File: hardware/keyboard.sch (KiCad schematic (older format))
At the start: 140 parts

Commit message: WIP schematic + PCB design
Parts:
- removed D? (x64): D, symbol D
- removed S? (x63): SPST, symbol SPST
- added D10, D11, D12, D13, D14, D15, D16, D17, D18, D19, D20, D21, D22, D23, D24, D25, D26, D27, D28, D29, D3, D30, D31, D32, D33, D34, D35, D36, D37, D38, D39, D4, D40, D41, D42, D43, D44, D45, D46, D47, D48, D49, D5, D50, D51, D52, D53, D54, D55, D56, D57, D58, D59, D6, D60, D61, D62, D63, D64, D65, D66, D7, D8, D9: D_Small, Diodes_SMD:D_1206, symbol D_Small
- added S10, S11, S12, S13, S14, S15, S16, S17, S18, S19, S2, S20, S21, S22, S23, S24, S25, S26, S27, S28, S29, S3, S30, S31, S32, S33, S34, S35, S36, S37, S38, S39, S4, S40, S41, S42, S43, S44, S45, S46, S47, S48, S49, S5, S50, S51, S52, S53, S54, S55, S56, S57, S58, S59, S6, S60, S61, S62, S63, S64, S7, S8, S9: SPST, keyboard-modules:CHERRY_PCB_100H, symbol SPST
- C1, C2, C3: renamed from C?; footprint (none) -> Capacitors_SMD:C_1206_HandSoldering
- D1: renamed from D?; footprint (none) -> LEDs:LED_1206
- D2: renamed from D?; footprint (none) -> Diodes_SMD:D_1206
- F1: renamed from F?; footprint (none) -> Fuse_Holders_and_Fuses:Fuse_SMD1206_HandSoldering
- J1: renamed from J?; footprint (none) -> Connectors_USB:USB_Micro-B_Molex-105017-0001
- R1, R2, R3: renamed from R?; footprint (none) -> Resistors_SMD:R_1206_HandSoldering
- S1: renamed from S?; footprint (none) -> keyboard-modules:CHERRY_PCB_100H
- U1: renamed from U?; footprint TQFP44 -> Housings_QFP:TQFP-44_10x10mm_Pitch0.8mm
- Y1: renamed from Y?; footprint (none) -> Crystals:Crystal_SMD_2012-2pin_2.0x1.2mm_HandSoldering
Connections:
- wire segments 168 -> 360
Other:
- moved on the sheet: S1

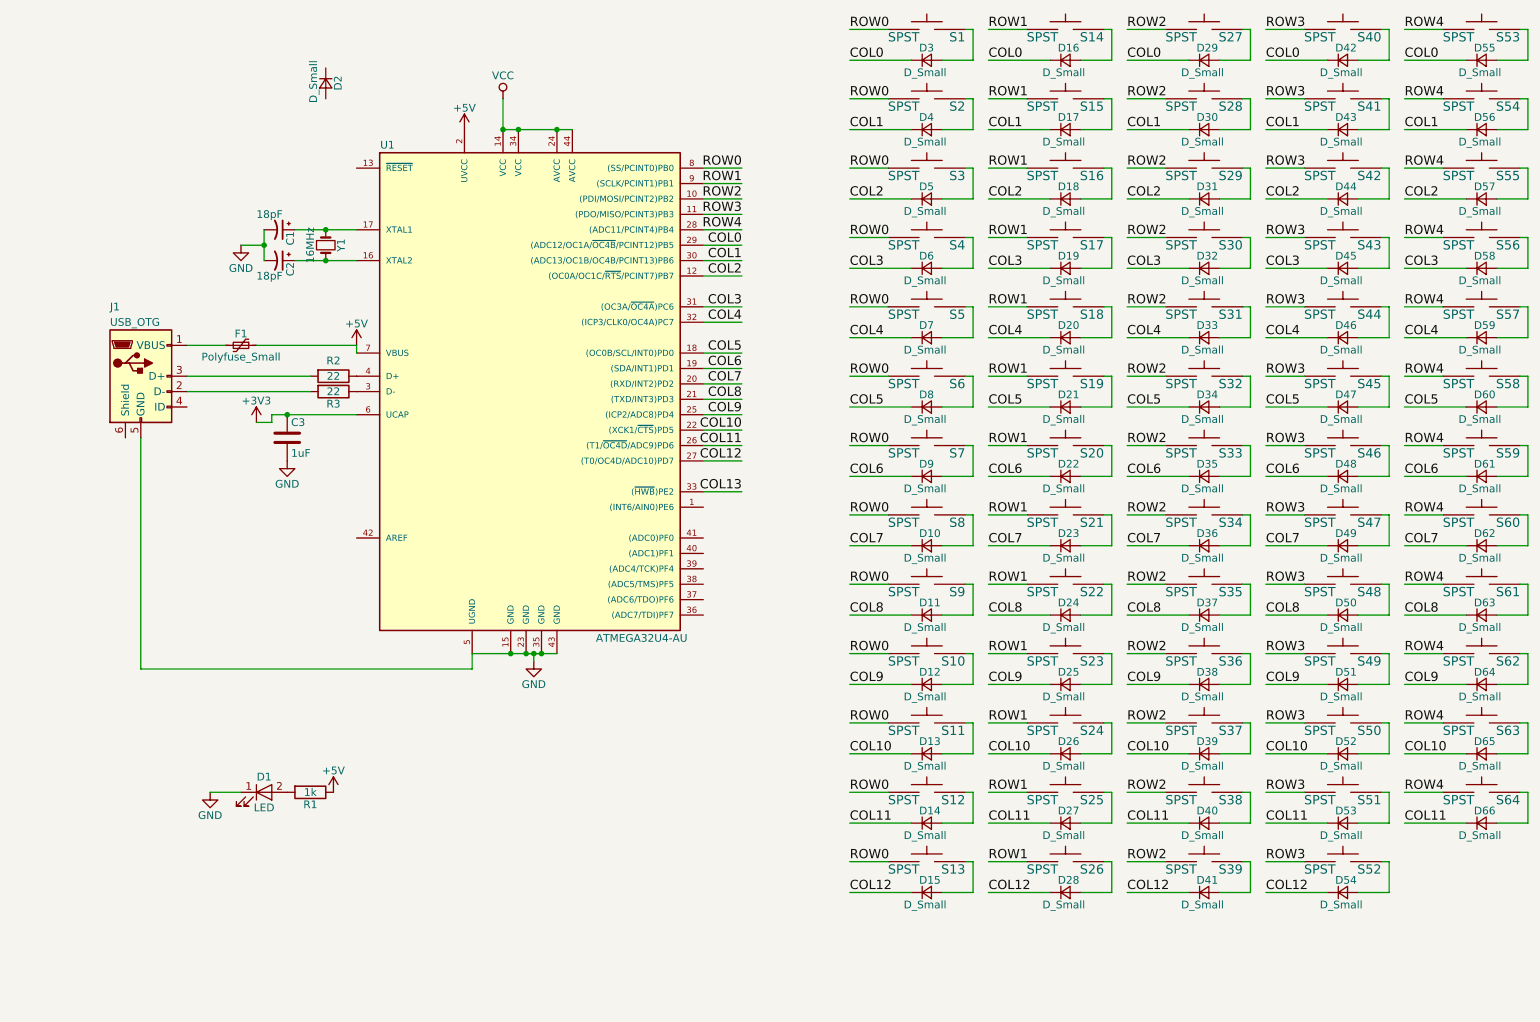
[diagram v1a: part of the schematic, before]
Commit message: Extract keys into sheets, add MCP23018
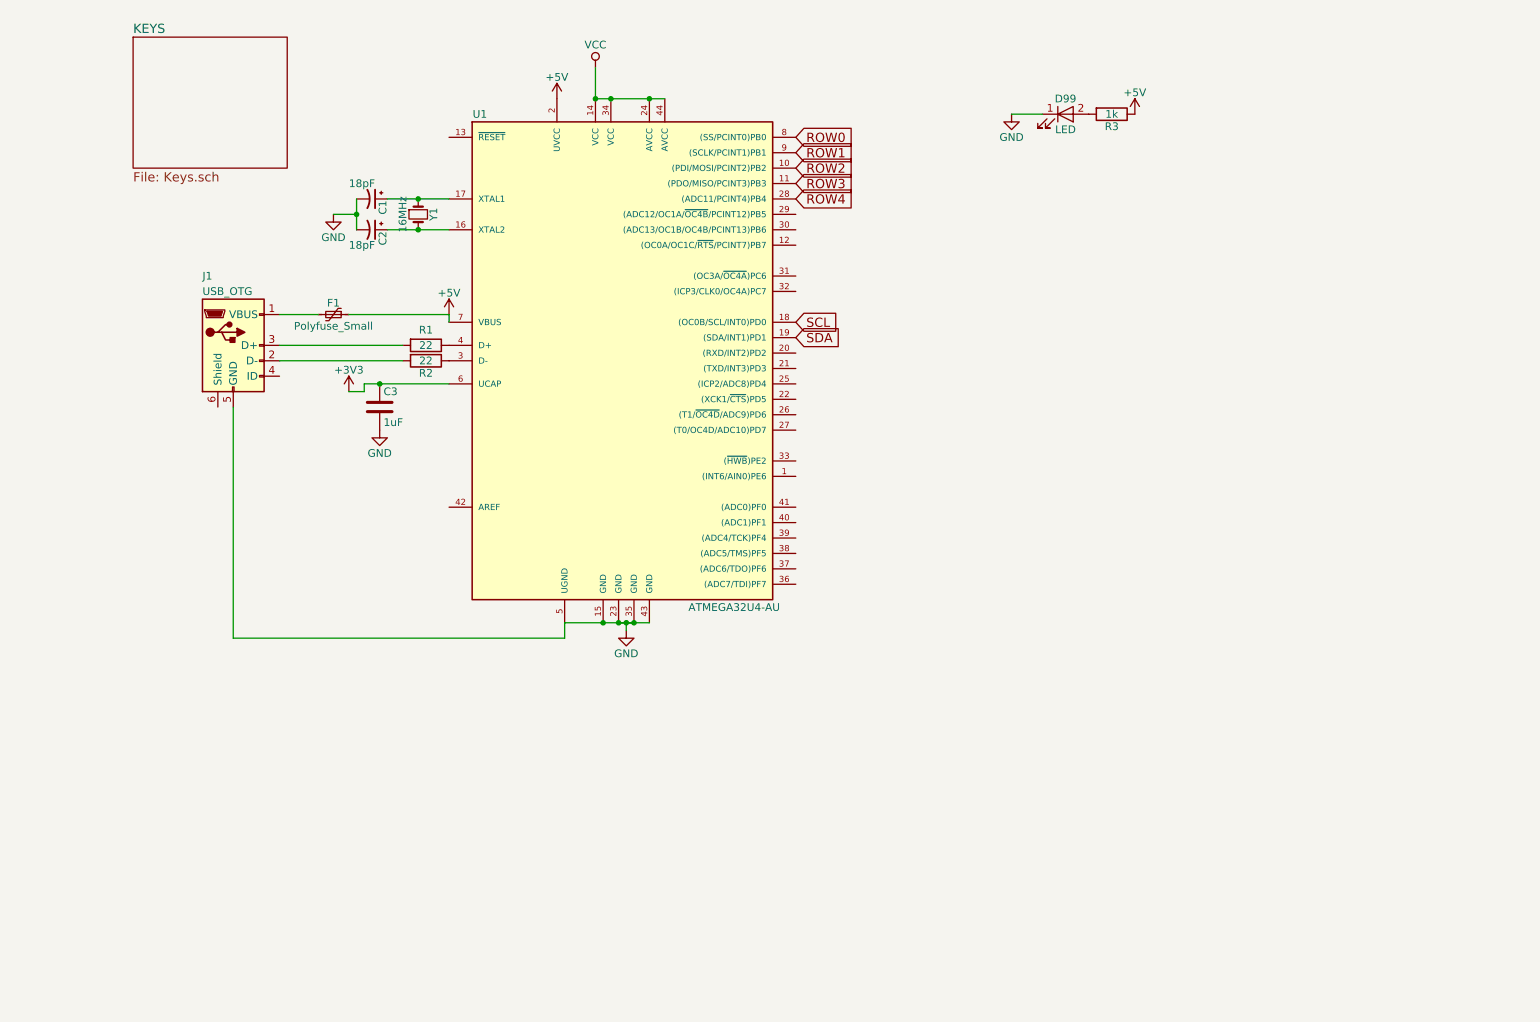
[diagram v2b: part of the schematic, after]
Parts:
- removed D10, D11, D12, D13, D14, D15, D16, D17, D18, D19, D2, D20, D21, D22, D23, D24, D25, D26, D27, D28, D29, D3, D30, D31, D32, D33, D34, D35, D36, D37, D38, D39, D4, D40, D41, D42, D43, D44, D45, D46, D47, D48, D49, D5, D50, D51, D52, D53, D54, D55, D56, D57, D58, D59, D6, D60, D61, D62, D63, D64, D65, D66, D7, D8, D9: D_Small, Diodes_SMD:D_1206, symbol D_Small
- removed S1, S10, S11, S12, S13, S14, S15, S16, S17, S18, S19, S2, S20, S21, S22, S23, S24, S25, S26, S27, S28, S29, S3, S30, S31, S32, S33, S34, S35, S36, S37, S38, S39, S4, S40, S41, S42, S43, S44, S45, S46, S47, S48, S49, S5, S50, S51, S52, S53, S54, S55, S56, S57, S58, S59, S6, S60, S61, S62, S63, S64, S7, S8, S9: SPST, keyboard-modules:CHERRY_PCB_100H, symbol SPST
- renumbered D1 to D99, R2 to R1, R3 to R2, R1 to R3
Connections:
- net COL0: no longer names the net of U1.29 ((ADC12/OC1A/~OC4B~/PCINT12)PB5)
- net COL1: no longer names the net of U1.30 ((ADC13/OC1B/OC4B/PCINT13)PB6)
- net COL10: no longer names the net of U1.22 ((XCK1/~CTS~)PD5)
- net COL11: no longer names the net of U1.26 ((T1/~OC4D~/ADC9)PD6)
- net COL12: no longer names the net of U1.27 ((T0/OC4D/ADC10)PD7)
- net COL13: no longer names the net of U1.33 ((~HWB~)PE2)
- net COL2: no longer names the net of U1.12 ((OC0A/OC1C/~RTS~/PCINT7)PB7)
- net COL3: no longer names the net of U1.31 ((OC3A/~OC4A~)PC6)
- net COL4: no longer names the net of U1.32 ((ICP3/CLK0/OC4A)PC7)
- net COL5 renamed SCL
- net COL6 renamed SDA
- net COL7: no longer names the net of U1.20 ((RXD/INT2)PD2)
- net COL8: no longer names the net of U1.21 ((TXD/INT3)PD3)
- net COL9: no longer names the net of U1.25 ((ICP2/ADC8)PD4)
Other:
- moved on the sheet: C1, C2, C3, D99, F1, J1, R1, R2, R3, U1, Y1

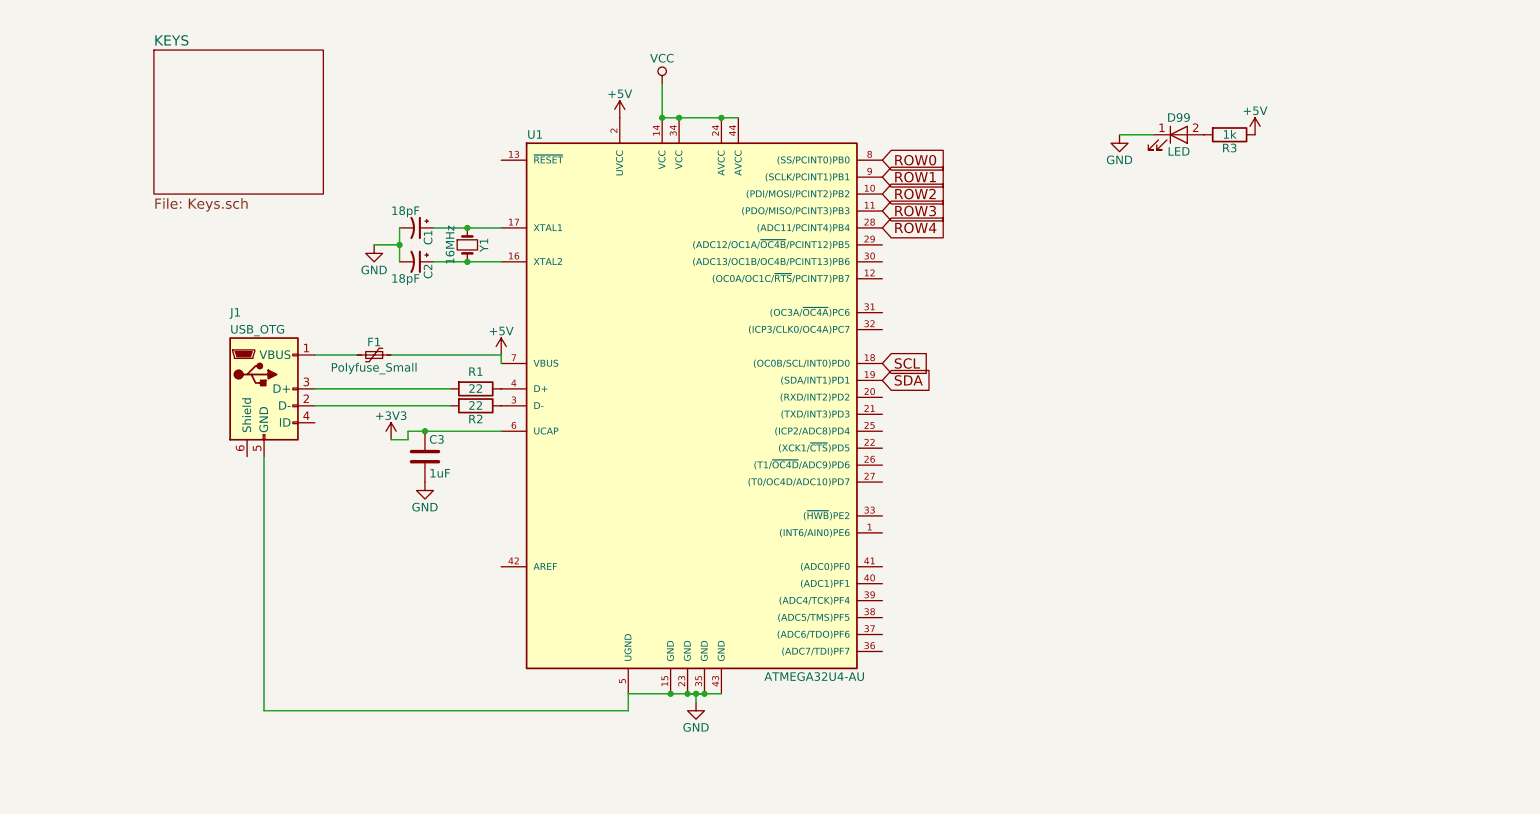
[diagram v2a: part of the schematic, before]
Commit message: Add HWB, breakouts, LED to sch
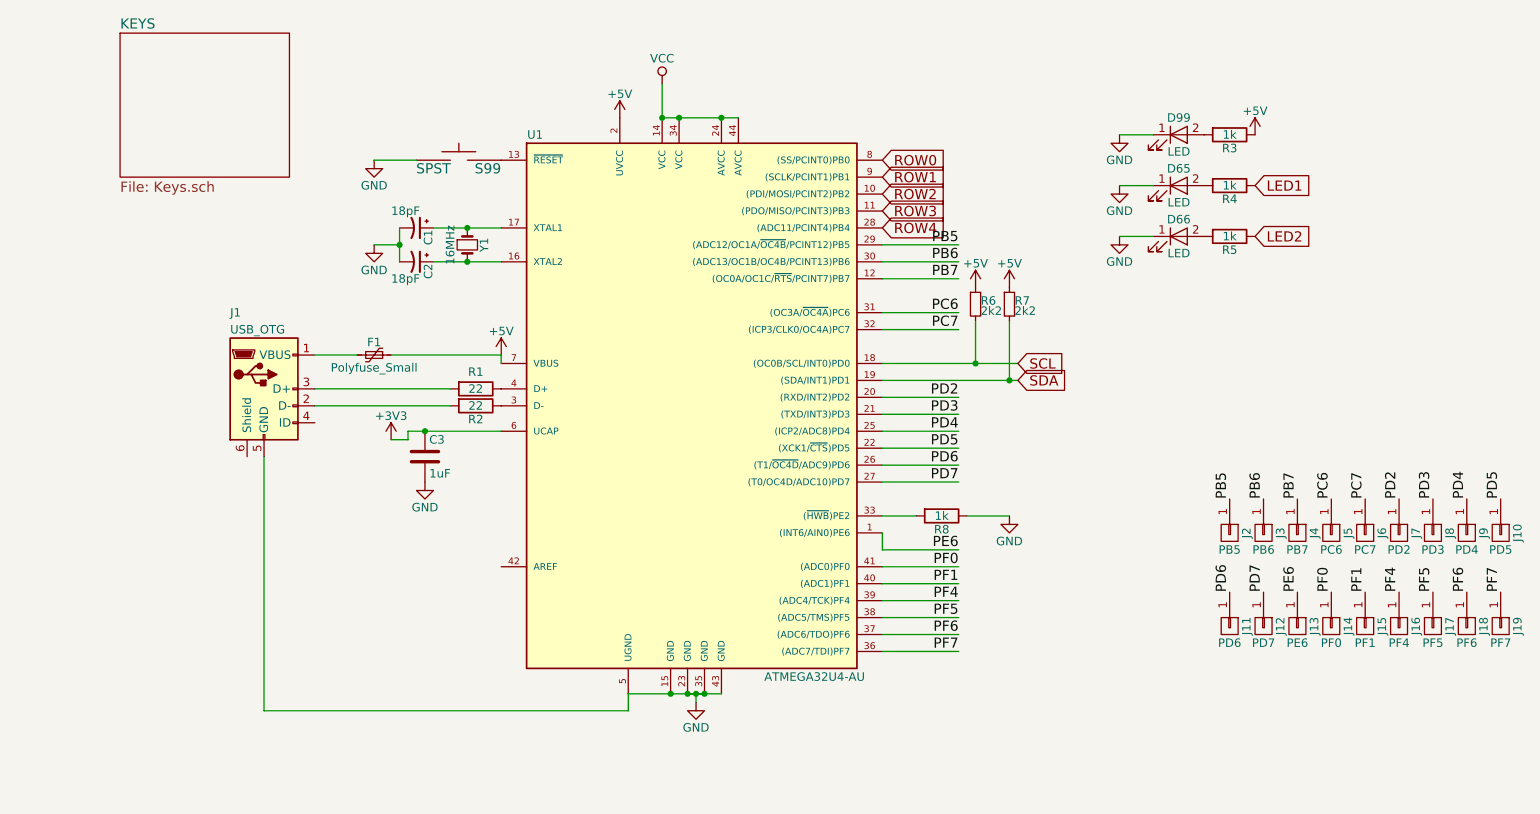
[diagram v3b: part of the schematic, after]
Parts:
- added D65, D66: LED, LEDs:LED_1206, symbol LED
- added J10: PD5, Connectors:1pin, symbol CONN_01X01
- added J11: PD6, Connectors:1pin, symbol CONN_01X01
- added J12: PD7, Connectors:1pin, symbol CONN_01X01
- added J13: PE6, Connectors:1pin, symbol CONN_01X01
- added J14: PF0, Connectors:1pin, symbol CONN_01X01
- added J15: PF1, Connectors:1pin, symbol CONN_01X01
- added J16: PF4, Connectors:1pin, symbol CONN_01X01
- added J17: PF5, Connectors:1pin, symbol CONN_01X01
- added J18: PF6, Connectors:1pin, symbol CONN_01X01
- added J19: PF7, Connectors:1pin, symbol CONN_01X01
- added J2: PB5, Connectors:1pin, symbol CONN_01X01
- added J3: PB6, Connectors:1pin, symbol CONN_01X01
- added J4: PB7, Connectors:1pin, symbol CONN_01X01
- added J5: PC6, Connectors:1pin, symbol CONN_01X01
- added J6: PC7, Connectors:1pin, symbol CONN_01X01
- added J7: PD2, Connectors:1pin, symbol CONN_01X01
- added J8: PD3, Connectors:1pin, symbol CONN_01X01
- added J9: PD4, Connectors:1pin, symbol CONN_01X01
- added R4, R5, R8: 1k, Resistors_SMD:R_1206_HandSoldering, symbol R
- added R6, R7: 2k2, Resistors_SMD:R_1206_HandSoldering, symbol R_Small
- added S99: SPST, Buttons_Switches_SMD:SW_SPST_EVQP0, symbol SPST
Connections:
- net +5V: now also R6.1, R7.1
- net GND: now also D65.1 (K), D66.1 (K), R8.1, S99.1
- net SCL: now also R6.2
- net SDA: now also R7.2
- net PE6: now reaches U1.1 ((INT6/AIN0)PE6)
- net PE6: now also J13.1 (P1)
- net PB7: now reaches U1.12 ((OC0A/OC1C/~RTS~/PCINT7)PB7)
- net PB7: now also J4.1 (P1)
- net at U1.13 (~RESET~): now also S99.2
- net PD2: now reaches U1.20 ((RXD/INT2)PD2)
- net PD2: now also J7.1 (P1)
- net PD3: now reaches U1.21 ((TXD/INT3)PD3)
- net PD3: now also J8.1 (P1)
- net PD5: now reaches U1.22 ((XCK1/~CTS~)PD5)
- net PD5: now also J10.1 (P1)
- net PD4: now reaches U1.25 ((ICP2/ADC8)PD4)
- net PD4: now also J9.1 (P1)
- net PD6: now reaches U1.26 ((T1/~OC4D~/ADC9)PD6)
- net PD6: now also J11.1 (P1)
- net PD7: now reaches U1.27 ((T0/OC4D/ADC10)PD7)
- net PD7: now also J12.1 (P1)
- net PB5: now reaches U1.29 ((ADC12/OC1A/~OC4B~/PCINT12)PB5)
- net PB5: now also J2.1 (P1)
- net PB6: now reaches U1.30 ((ADC13/OC1B/OC4B/PCINT13)PB6)
- net PB6: now also J3.1 (P1)
- net PC6: now reaches U1.31 ((OC3A/~OC4A~)PC6)
- net PC6: now also J5.1 (P1)
- net PC7: now reaches U1.32 ((ICP3/CLK0/OC4A)PC7)
- net PC7: now also J6.1 (P1)
- net at U1.33 ((~HWB~)PE2): now also R8.2
- net PF7: now reaches U1.36 ((ADC7/TDI)PF7)
- net PF7: now also J19.1 (P1)
- net PF6: now reaches U1.37 ((ADC6/TDO)PF6)
- net PF6: now also J18.1 (P1)
- net PF5: now reaches U1.38 ((ADC5/TMS)PF5)
- net PF5: now also J17.1 (P1)
- net PF4: now reaches U1.39 ((ADC4/TCK)PF4)
- net PF4: now also J16.1 (P1)
- net PF1: now reaches U1.40 ((ADC1)PF1)
- net PF1: now also J15.1 (P1)
- net PF0: now reaches U1.41 ((ADC0)PF0)
- net PF0: now also J14.1 (P1)
- new net: D65.2 (A), R4.2
- new net: D66.2 (A), R5.2
- new net LED1: R4.1
- new net LED2: R5.1
